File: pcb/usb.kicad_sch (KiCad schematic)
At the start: 16 parts, among them J4 USB4105, SW2 PBH2UEESNPNAGX, U147 AP2112K-3.3, U149 74LVC1G17GW,125, U151 74LVC1G80

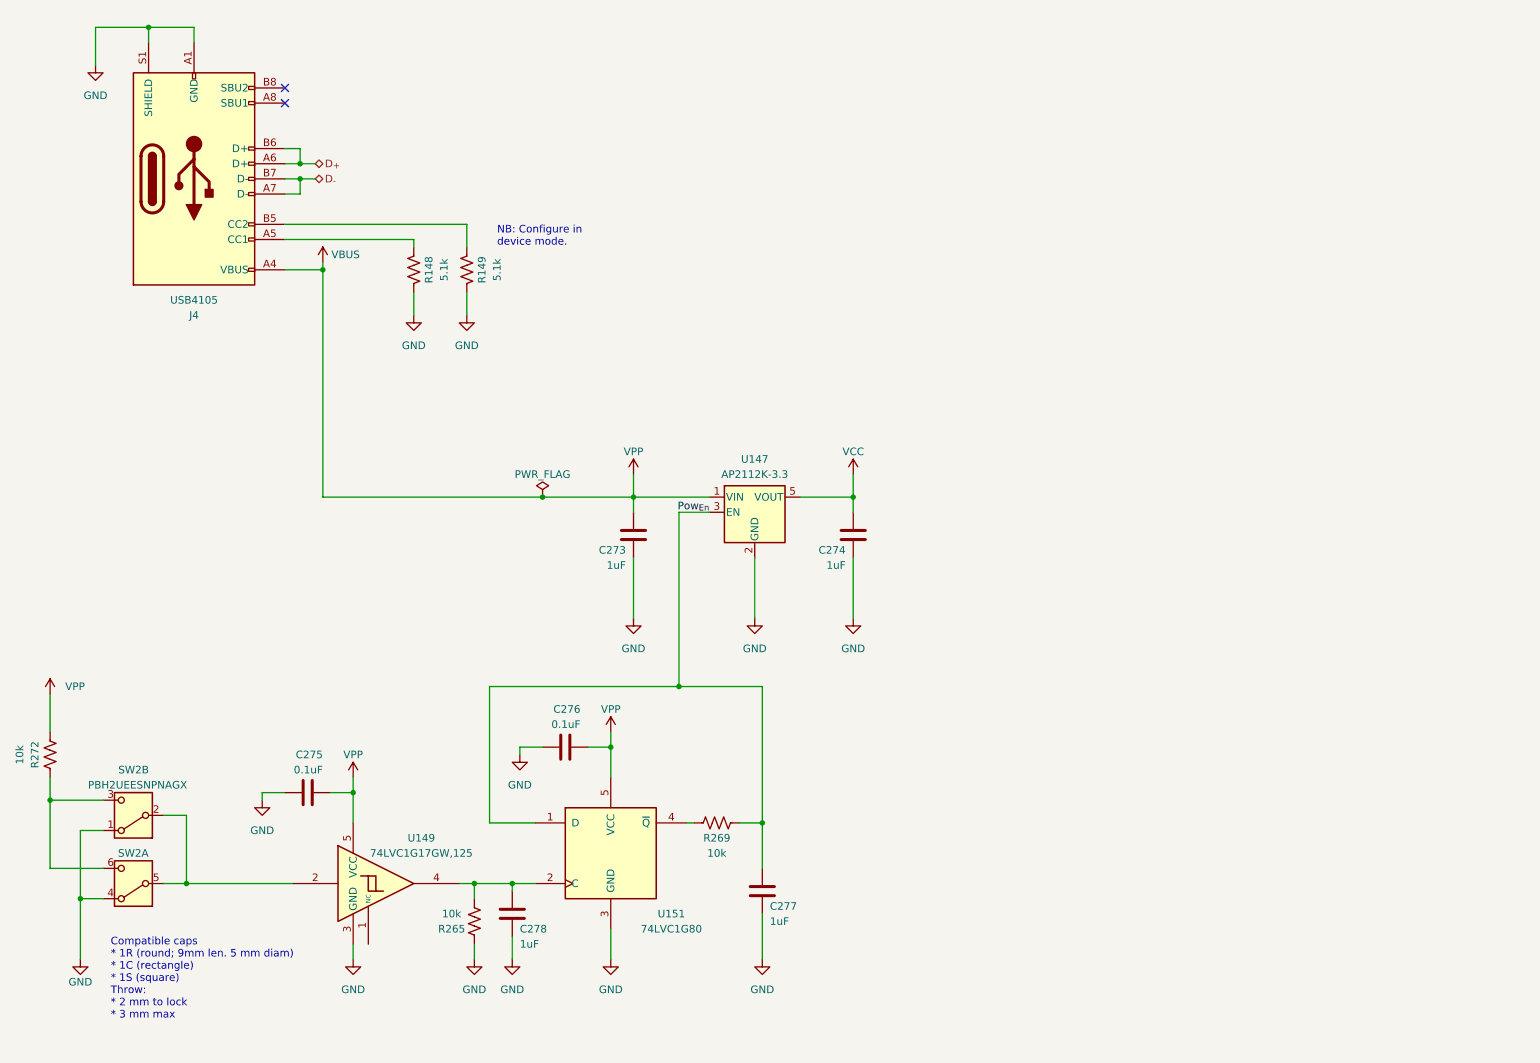
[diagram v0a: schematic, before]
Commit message: Finished schematic, started routing
- There is a 8-channel motif that will need to be copied 16x on the
  board. I'm not sure the most efficient way to do this.
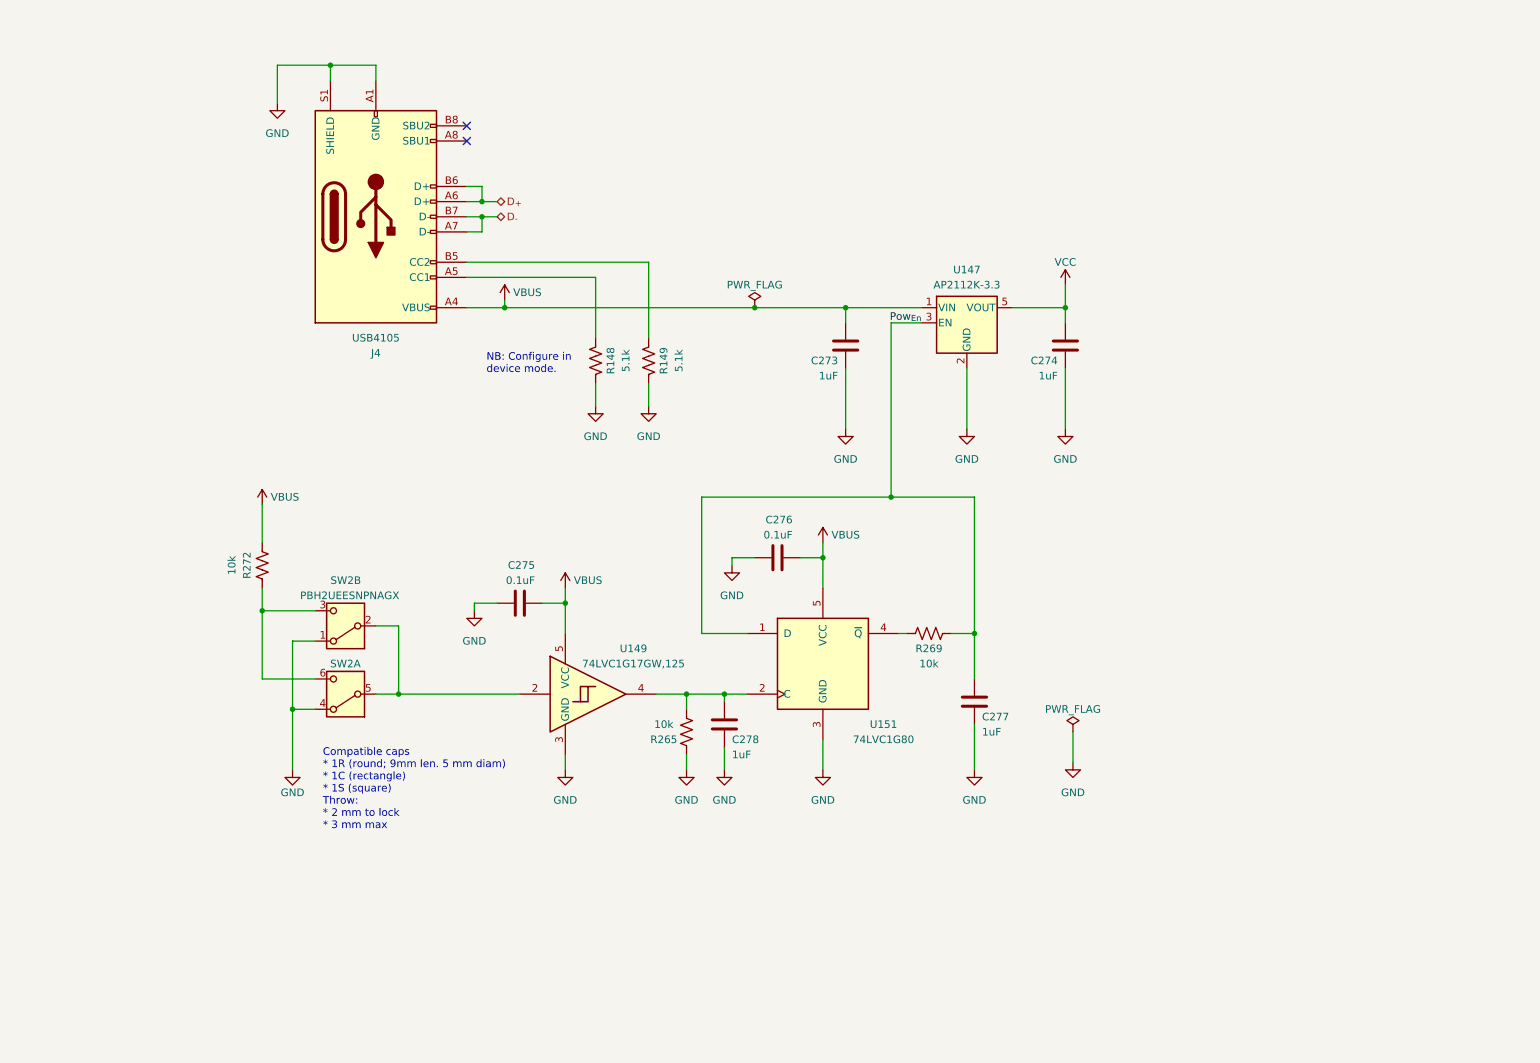
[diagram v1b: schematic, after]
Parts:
- J4: symbol Connector:USB_C_Receptacle_USB2.0 -> Connector:USB_C_Receptacle_USB2.0_16P
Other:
- moved on the sheet: C273, C274, C275, C276, C277, C278, J4, R148, R149, R265, R269, R272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

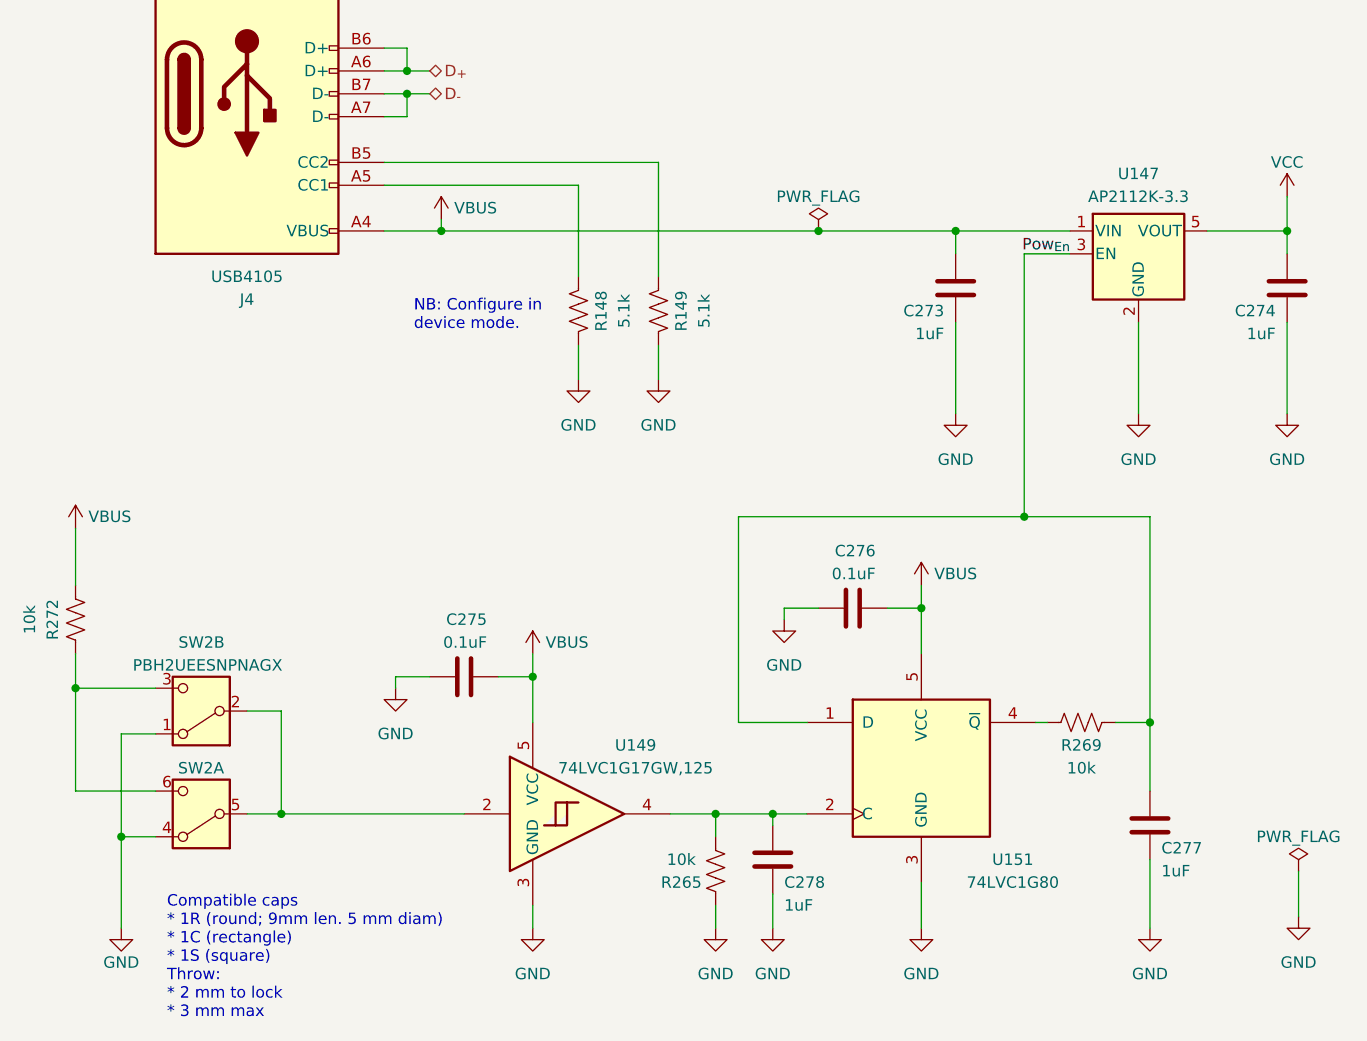
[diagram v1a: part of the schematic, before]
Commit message: Motif is repeated
- some components are grouped by function
- components are roughly organized within groups
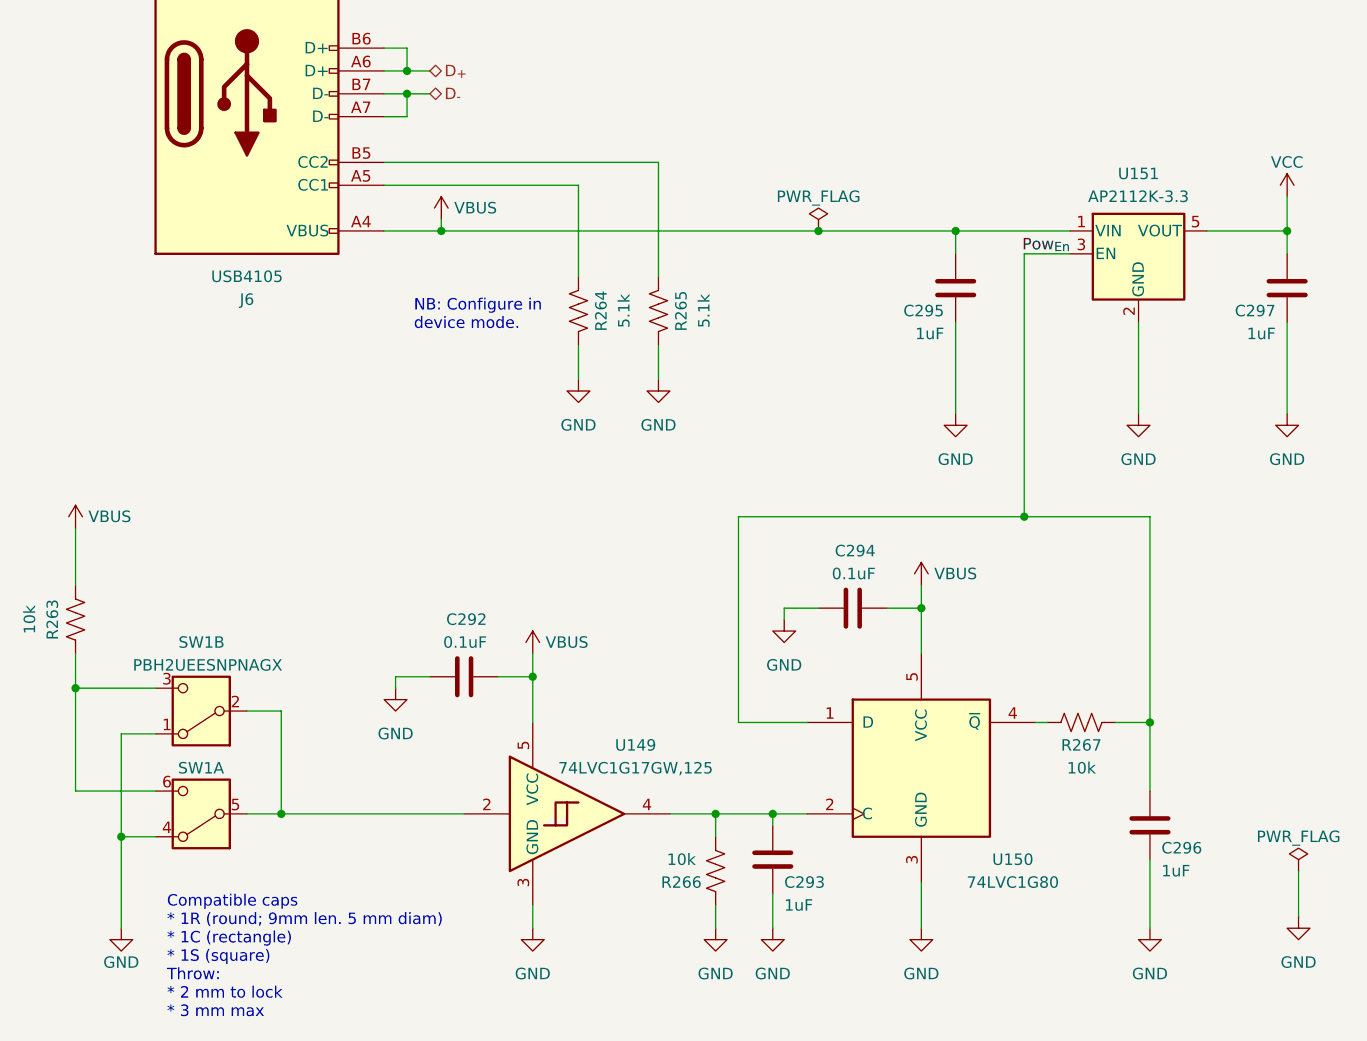
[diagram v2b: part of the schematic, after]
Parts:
- renumbered C275 to C292, C278 to C293, C276 to C294, C273 to C295, C277 to C296, C274 to C297, J4 to J6, R272 to R263, R148 to R264, R149 to R265, R265 to R266, R269 to R267, SW2 to SW1, U151 to U150, U147 to U151

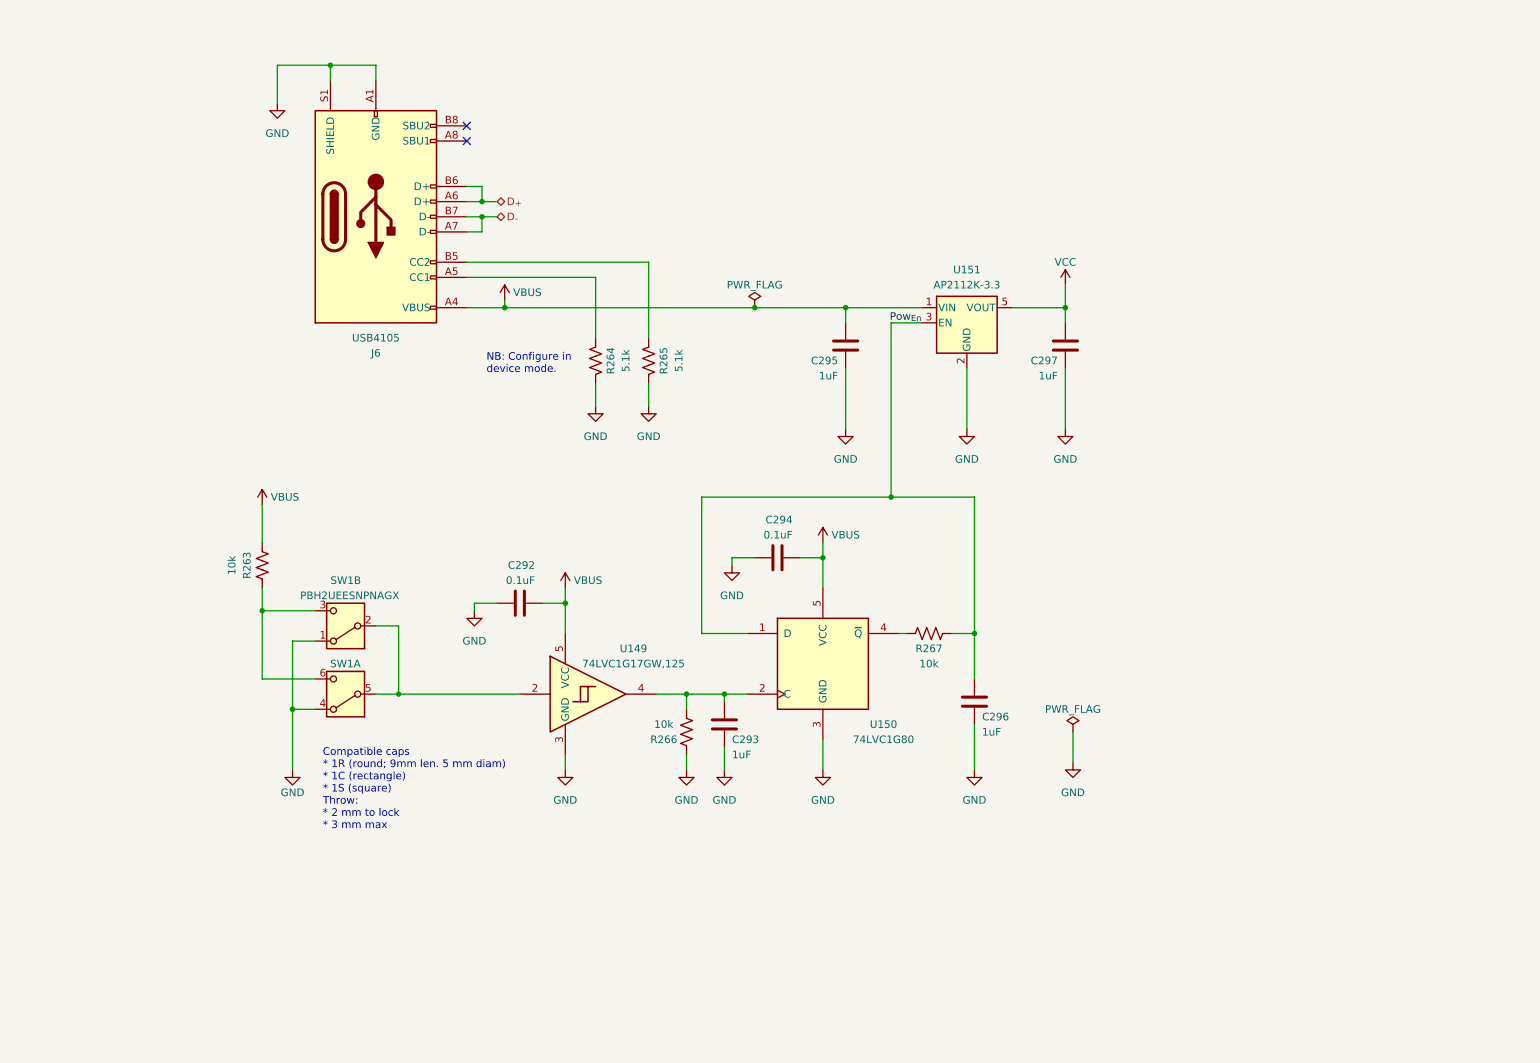
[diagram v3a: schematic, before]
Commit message: Added user IO and battery
- Battery provides noise free operation
- OLED display and rotary encoder are not that hard to use
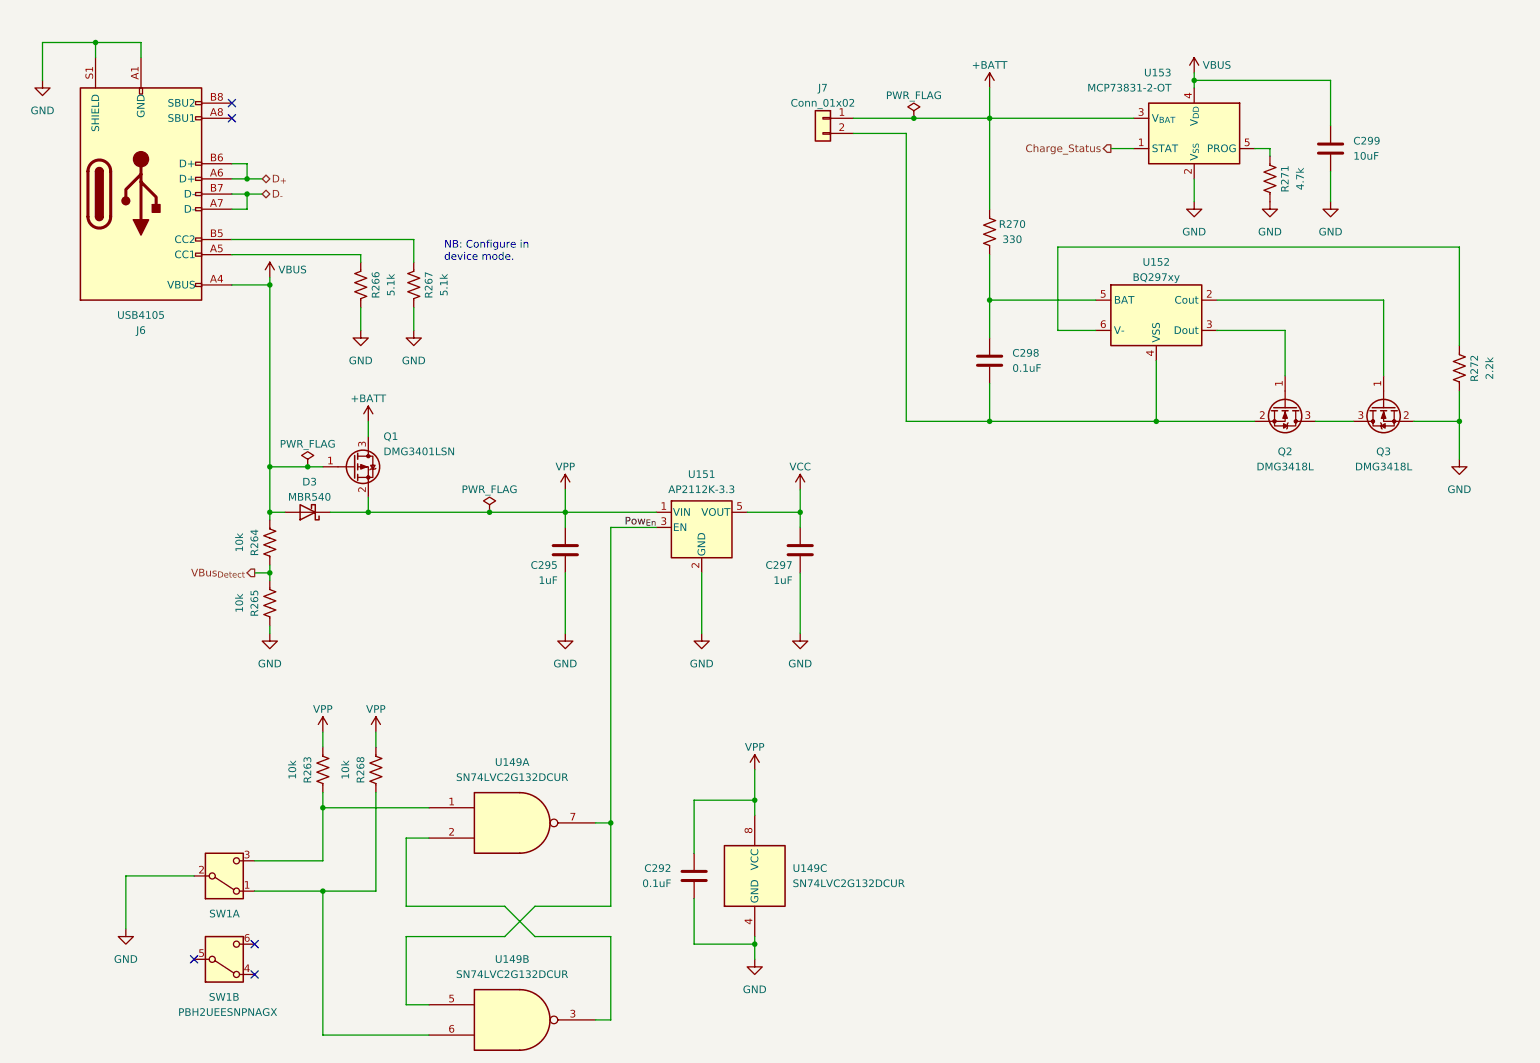
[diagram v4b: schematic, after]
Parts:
- removed C293, C296: 1uF, Capacitor_SMD:C_0603_1608Metric, symbol Device:C
- removed C294: 0.1uF, Capacitor_SMD:C_0402_1005Metric, symbol Device:C
- removed U149: 74LVC1G17GW,125, Package_TO_SOT_SMD:SOT-353_SC-70-5, symbol 74xGxx:74LVC1G17
- removed U150: 74LVC1G80, Package_TO_SOT_SMD:SOT-353_SC-70-5, symbol 74xGxx:74LVC1G80
- added C298: 0.1uF, Capacitor_SMD:C_0402_1005Metric, symbol Device:C
- added C299: 10uF, Capacitor_SMD:C_0805_2012Metric, symbol Device:C
- added D3: MBR540, Diode_SMD:D_SOD-123, symbol Device:D_Schottky
- added J7: Conn_01x02, Connector_JST:JST_PH_S2B-PH-SM4-TB_1x02-1MP_P2.00mm_Horizontal, symbol Connector_Generic:Conn_01x02
- added Q1: DMG3401LSN, Package_TO_SOT_SMD:SOT-23, symbol Transistor_FET:DMG2301L
- added Q2, Q3: DMG3418L, Package_TO_SOT_SMD:SOT-23, symbol Transistor_FET:DMG3414U
- added R268: 10k, Resistor_SMD:R_0402_1005Metric, symbol Device:R_US
- added R270: 330, Resistor_SMD:R_0603_1608Metric, symbol Device:R_US
- added R271: 4.7k, Resistor_SMD:R_0402_1005Metric, symbol Device:R_US
- added R272: 2.2k, Resistor_SMD:R_0402_1005Metric, symbol Device:R_US
- added U149: SN74LVC2G132DCUR, Package_SO:VSSOP-8_2.3x2mm_P0.5mm, symbol 74xGxx:74LVC2G00
- added U152: BQ297xy, Package_SON:WSON-6_1.5x1.5mm_P0.5mm, symbol Battery_Management:BQ297xy
- added U153: MCP73831-2-OT, Package_TO_SOT_SMD:SOT-23-5, symbol Battery_Management:MCP73831-2-OT
- R264, R265: value 5.1k -> 10k
- R266, R267: value 10k -> 5.1k
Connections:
- net GND: now also R267.2, SW1.2 (B), C299.2, Q3.2 (S), R271.1, R272.1, U149.4 (GND), U153.2 (V_{SS}); no longer R264.2, SW1.1 (A), SW1.4 (A)
- net Pow_{En}: now also U149.5, U149.7; no longer R267.2
- net VBUS: now also R264.1, C299.1, D3.2 (A), Q1.1 (G), U153.4 (V_{DD}); no longer C292.1, C295.1, R263.1, U151.1 (VIN)
- net at R266.1: now also J6.A5 (CC1)
- net at J6.B5 (CC2): now also R267.1; no longer R265.1
- net at SW1.5 (B): no longer SW1.2 (B)
- net at R263.2, SW1.3 (C): now also U149.1; no longer SW1.6 (C)
- new net: Q3.1 (G), U152.2 (Cout)
- new net: Q2.3 (D), Q3.3 (D)
- new net: R272.2, U152.6 (V-)
- new net: C298.1, R270.1, U152.5 (BAT)
- new net: C298.2, J7.2 (Pin_2), Q2.2 (S), U152.4 (VSS)
- new net: R268.2, SW1.1 (A), U149.6
- new net: U149.2, U149.3
- new net: R271.2, U153.5 (PROG)
- new net: Q2.1 (G), U152.3 (Dout)
- new net +BATT: J7.1 (Pin_1), Q1.3 (D), R270.2, U153.3 (V_{BAT})
- new net Charge_Status: U153.1 (STAT)
- new net VBus_{Detect}: R264.2, R265.1
- new net VPP: C292.1, C295.1, D3.1 (K), Q1.2 (S), R263.1, R268.1, U149.8 (VCC), U151.1 (VIN)
- no-connect marks 2 -> 5
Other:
- note removed: "Compatible caps * 1R (round; 9mm len. 5 mm diam) * 1C (rectangle) * 1S (square) Throw: * 2 mm to lock * 3 mm max"
